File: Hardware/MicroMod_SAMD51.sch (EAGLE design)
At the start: 30 parts, among them J2 MICROMOD-2222, U1 W25QXX6X5, U2 ATSAMD51J20A-A, Y1 32.768kHz

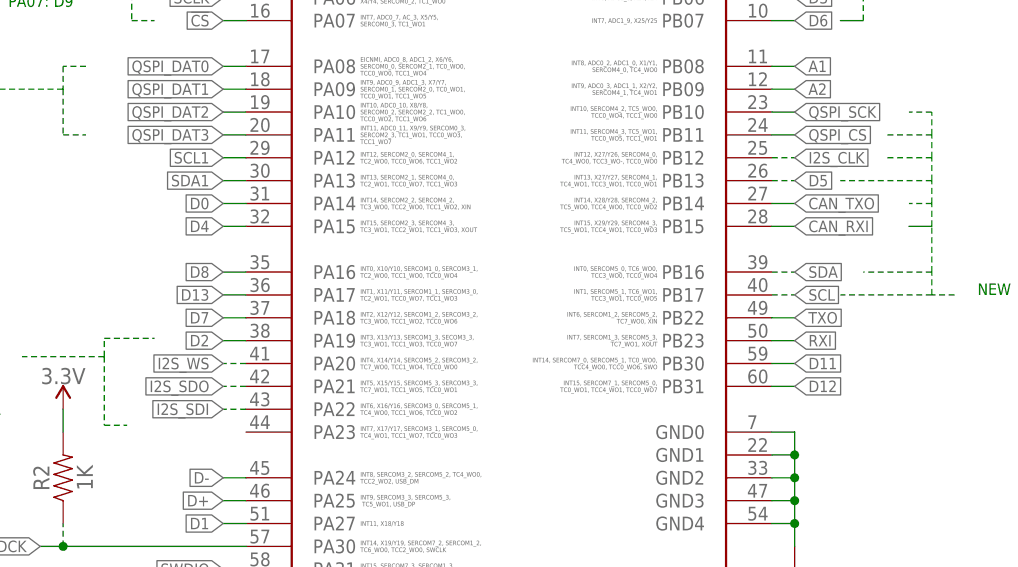
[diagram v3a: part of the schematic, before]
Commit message: Puts i2c on correct pin
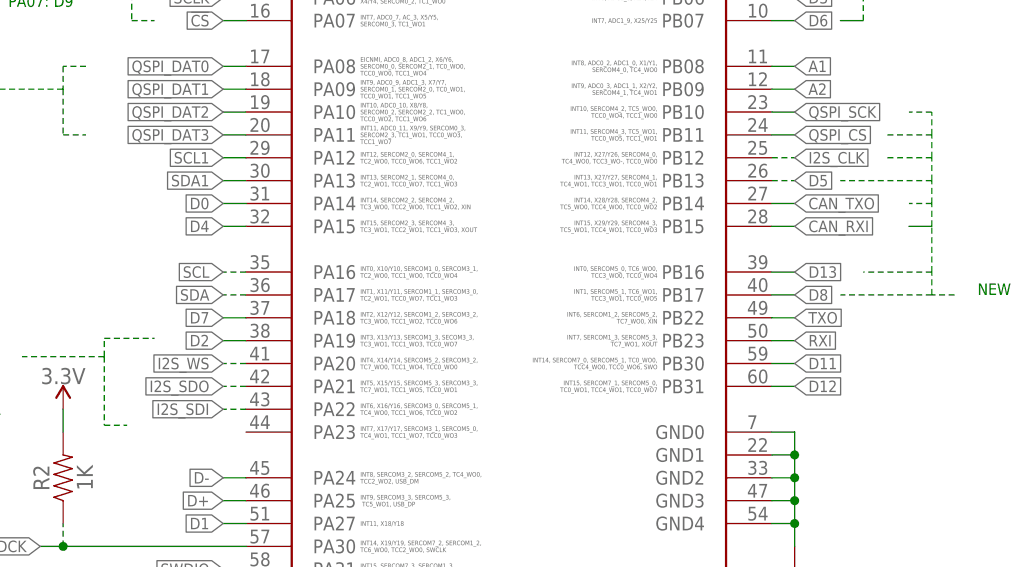
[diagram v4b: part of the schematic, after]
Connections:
- net D13: now also U2.PB16; no longer U2.PA17
- net D8: now also U2.PB17; no longer U2.PA16
- net SCL: now also U2.PA16; no longer U2.PB17
- net SDA: now also U2.PA17; no longer U2.PB16
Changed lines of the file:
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@@
 <net name="D13" class="0">
-<segment>
-<pinref part="U2" gate="G$1" pin="PA17"/>
-<wire x1="93.98" y1="193.04" x2="91.44" y2="193.04" width="0.1524" layer="91"/>
-<label x="91.44" y="193.04" size="1.27" layer="95" font="vector" rot="R180" xref="yes"/>
-</segment>
 <segment>
 <pinref part="R3" gate="G$1" pin="2"/>
@@
 <wire x1="187.96" y1="78.74" x2="185.42" y2="78.74" width="0.1524" layer="91"/>
 <label x="185.42" y="78.74" size="1.27" layer="95" rot="R180" xref="yes"/>
+</segment>
+<segment>
+<wire x1="152.4" y1="195.58" x2="154.94" y2="195.58" width="0.1524" layer="91"/>
+<label x="154.94" y="195.58" size="1.27" layer="95" font="vector" xref="yes"/>
+<pinref part="U2" gate="G$1" pin="PB16"/>
 </segment>
 </net>
@@
 <net name="D8" class="0">
 <segment>
-<pinref part="U2" gate="G$1" pin="PA16"/>
-<wire x1="93.98" y1="195.58" x2="91.44" y2="195.58" width="0.1524" layer="91"/>
-<label x="91.44" y="195.58" size="1.27" layer="95" font="vector" rot="R180" xref="yes"/>
-</segment>
-<segment>
 <wire x1="373.38" y1="165.1" x2="375.92" y2="165.1" width="0.1524" layer="91"/>
 <label x="375.92" y="165.1" size="1.27" layer="95" xref="yes"/>
 <pinref part="J2" gate="J1" pin="G6/BUS6"/>
+</segment>
+<segment>
+<wire x1="152.4" y1="193.04" x2="154.94" y2="193.04" width="0.1524" layer="91"/>
+<label x="154.94" y="193.04" size="1.27" layer="95" font="vector" xref="yes"/>
+<pinref part="U2" gate="G$1" pin="PB17"/>
 </segment>
 </net>
@@
 </segment>
 <segment>
-<pinref part="U2" gate="G$1" pin="PB17"/>
-<wire x1="152.4" y1="193.04" x2="154.94" y2="193.04" width="0.1524" layer="91" style="dashdot"/>
-<label x="154.94" y="193.04" size="1.27" layer="95" xref="yes"/>
+<wire x1="93.98" y1="195.58" x2="91.44" y2="195.58" width="0.1524" layer="91" style="dashdot"/>
+<label x="91.44" y="195.58" size="1.27" layer="95" rot="R180" xref="yes"/>
+<pinref part="U2" gate="G$1" pin="PA16"/>
 </segment>
 </net>
@@
 </segment>
 <segment>
-<pinref part="U2" gate="G$1" pin="PB16"/>
-<wire x1="152.4" y1="195.58" x2="154.94" y2="195.58" width="0.1524" layer="91" style="dashdot"/>
-<label x="154.94" y="195.58" size="1.27" layer="95" xref="yes"/>
+<wire x1="93.98" y1="193.04" x2="91.44" y2="193.04" width="0.1524" layer="91" style="dashdot"/>
+<label x="91.44" y="193.04" size="1.27" layer="95" rot="R180" xref="yes"/>
+<pinref part="U2" gate="G$1" pin="PA17"/>
 </segment>
 </net>

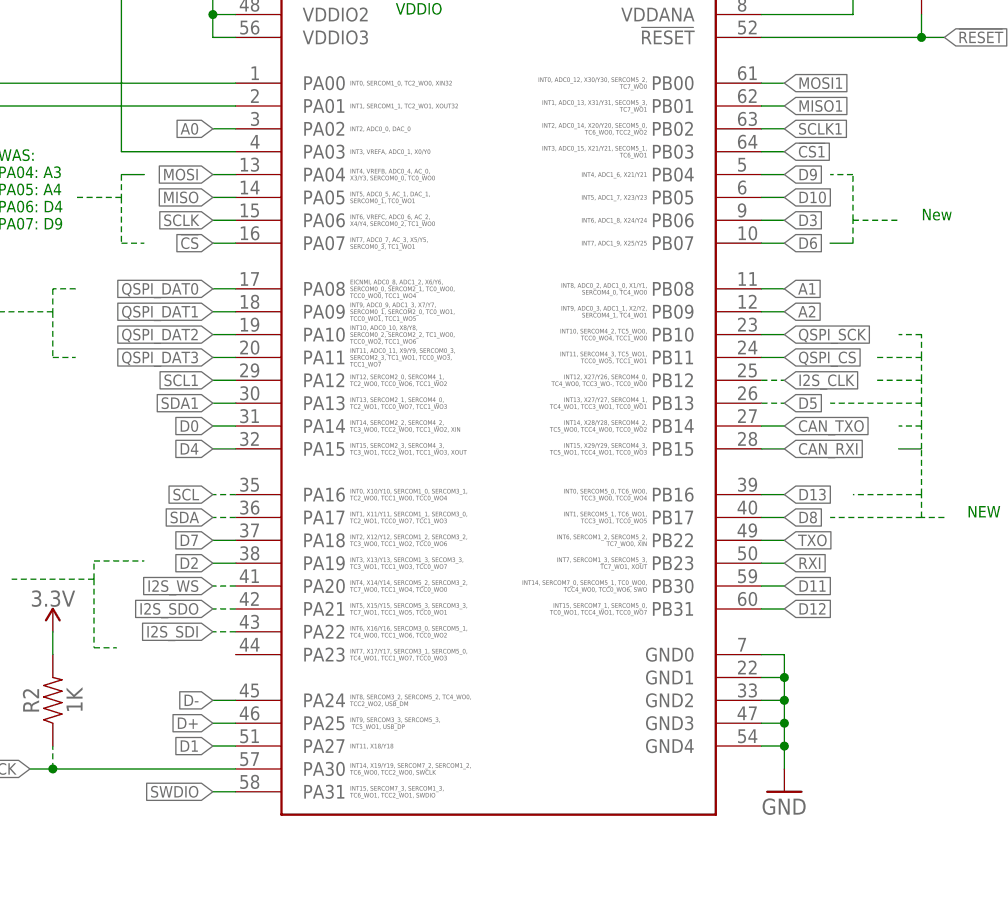
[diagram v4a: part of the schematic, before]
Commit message: Renumbers pins
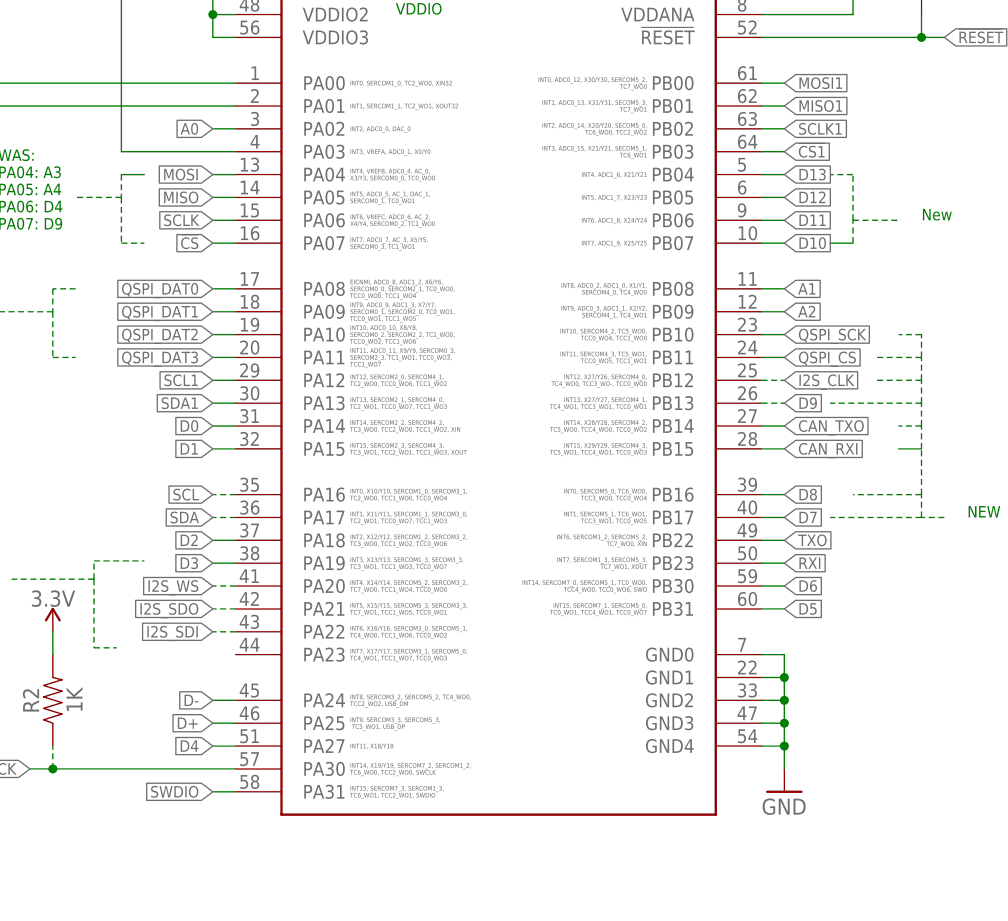
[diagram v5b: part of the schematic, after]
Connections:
- net D1: now also U2.PA15; no longer U2.PA27
- net D10: now also U2.PB07; no longer U2.PB05
- net D11: now also U2.PB06; no longer U2.PB30
- net D12: now also U2.PB05; no longer U2.PB31
- net D13: now also U2.PB04; no longer U2.PB16
- net D2: now also U2.PA18; no longer U2.PA19
- net D3: now also U2.PA19; no longer U2.PB06
- net D4: now also U2.PA27; no longer U2.PA15
- net D5: now also U2.PB31; no longer U2.PB13
- net D6: now also U2.PB30; no longer U2.PB07
- net D7: now also U2.PB17; no longer U2.PA18
- net D8: now also U2.PB16; no longer U2.PB17
- net D9: now also U2.PB13; no longer U2.PB04

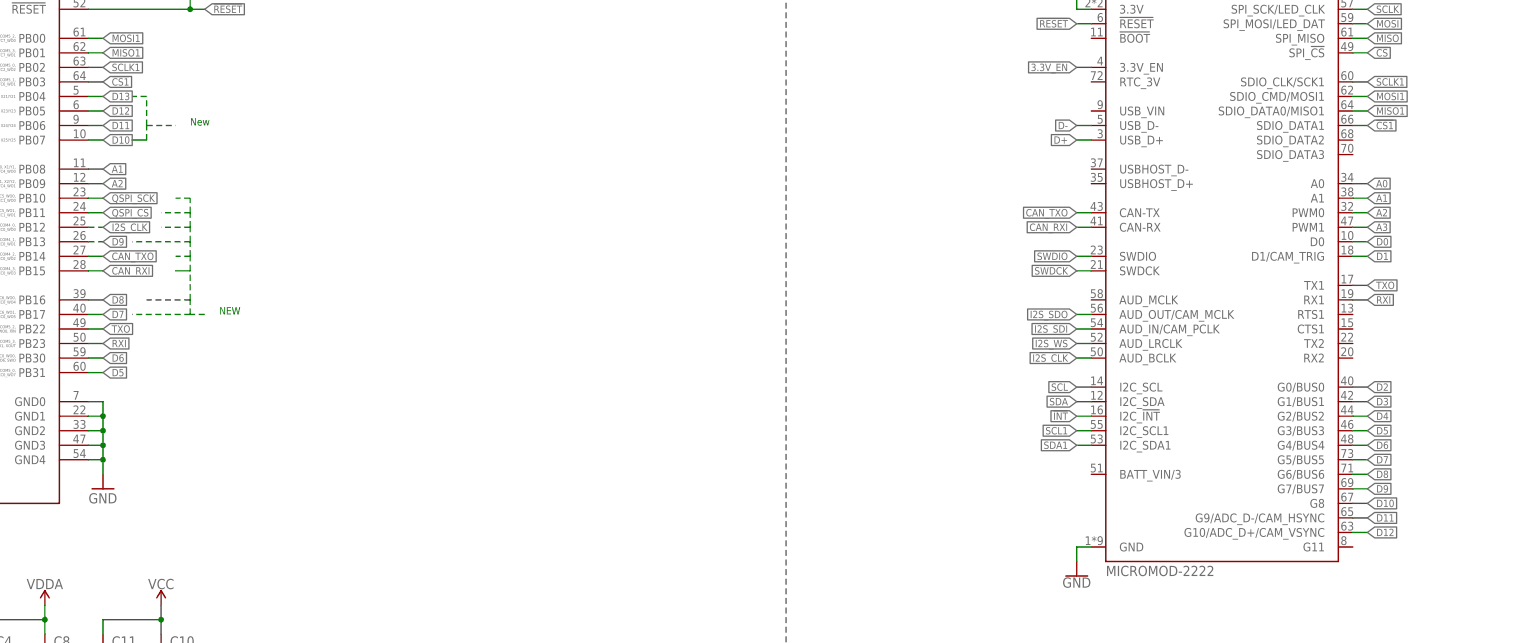
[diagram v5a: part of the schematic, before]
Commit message: Adds A3 to SAMD51, adds PWM to A2 and A3 net names
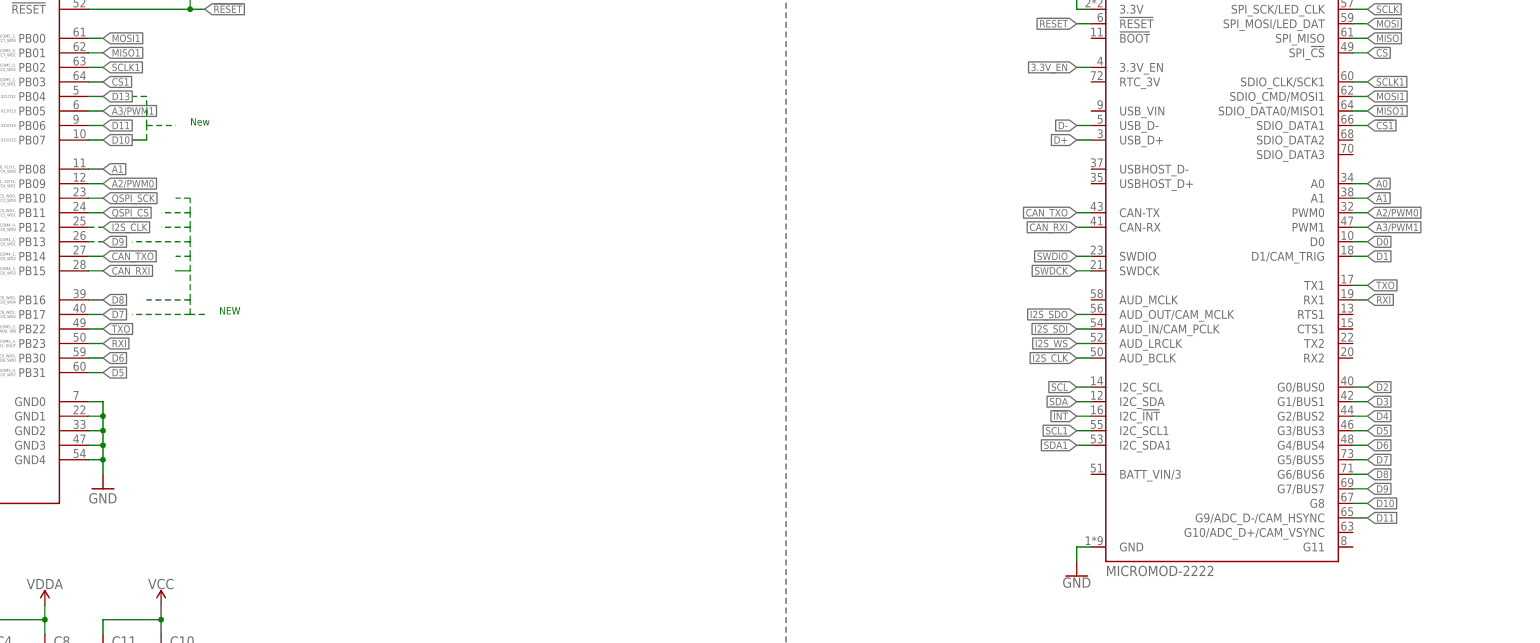
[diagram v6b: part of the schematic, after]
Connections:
- net A2 renamed A2/PWM0
- removed net A3: J2.PWM1
- removed net D12: J2.G10/ADC_D+/CAM_VSYNC, U2.PB05
- new net A3/PWM1: J2.PWM1, U2.PB05
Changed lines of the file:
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@@
-</segment>
-</net>
-<net name="A2" class="0">
-<segment>
-<pinref part="U2" gate="G$1" pin="PB09"/>
-<wire x1="152.4" y1="215.9" x2="154.94" y2="215.9" width="0.1524" layer="91"/>
-<label x="154.94" y="215.9" size="1.27" layer="95" font="vector" xref="yes"/>
-</segment>
-<segment>
-<pinref part="J2" gate="J1" pin="PWM0"/>
-<wire x1="373.38" y1="210.82" x2="375.92" y2="210.82" width="0.1524" layer="91"/>
-<label x="375.92" y="210.82" size="1.27" layer="95" xref="yes"/>
 </segment>
 </net>
@@
 </segment>
 </net>
-<net name="A3" class="0">
+<net name="D11" class="0">
+<segment>
+<pinref part="J2" gate="J1" pin="G9/ADC_D-/CAM_HSYNC"/>
+<wire x1="373.38" y1="157.48" x2="375.92" y2="157.48" width="0.1524" layer="91"/>
+<label x="375.92" y="157.48" size="1.27" layer="95" xref="yes"/>
+</segment>
+<segment>
+<pinref part="U2" gate="G$1" pin="PB06"/>
+<wire x1="152.4" y1="226.06" x2="154.94" y2="226.06" width="0.1524" layer="91"/>
+<label x="154.94" y="226.06" size="1.27" layer="95" xref="yes"/>
+</segment>
+</net>
+<net name="A3/PWM1" class="0">
+<segment>
+<pinref part="U2" gate="G$1" pin="PB05"/>
+<wire x1="152.4" y1="228.6" x2="154.94" y2="228.6" width="0.1524" layer="91"/>
+<label x="154.94" y="228.6" size="1.27" layer="95" xref="yes"/>
+</segment>
 <segment>
 <pinref part="J2" gate="J1" pin="PWM1"/>
@@
 </segment>
 </net>
-<net name="D11" class="0">
-<segment>
-<pinref part="J2" gate="J1" pin="G9/ADC_D-/CAM_HSYNC"/>
-<wire x1="373.38" y1="157.48" x2="375.92" y2="157.48" width="0.1524" layer="91"/>
-<label x="375.92" y="157.48" size="1.27" layer="95" xref="yes"/>
-</segment>
-<segment>
-<pinref part="U2" gate="G$1" pin="PB06"/>
-<wire x1="152.4" y1="226.06" x2="154.94" y2="226.06" width="0.1524" layer="91"/>
-<label x="154.94" y="226.06" size="1.27" layer="95" xref="yes"/>
-</segment>
-</net>
-<net name="D12" class="0">
-<segment>
-<pinref part="J2" gate="J1" pin="G10/ADC_D+/CAM_VSYNC"/>
-<wire x1="373.38" y1="154.94" x2="375.92" y2="154.94" width="0.1524" layer="91"/>
-<label x="375.92" y="154.94" size="1.27" layer="95" xref="yes"/>
-</segment>
-<segment>
-<pinref part="U2" gate="G$1" pin="PB05"/>
-<wire x1="152.4" y1="228.6" x2="154.94" y2="228.6" width="0.1524" layer="91"/>
-<label x="154.94" y="228.6" size="1.27" layer="95" xref="yes"/>
-</segment>
-</net>
 <net name="SCL1" class="0">
 <segment>
@@
 </segment>
 </net>
+<net name="A2/PWM0" class="0">
+<segment>
+<pinref part="J2" gate="J1" pin="PWM0"/>
+<wire x1="373.38" y1="210.82" x2="375.92" y2="210.82" width="0.1524" layer="91"/>
+<label x="375.92" y="210.82" size="1.27" layer="95" xref="yes"/>
+</segment>
+<segment>
+<pinref part="U2" gate="G$1" pin="PB09"/>
+<wire x1="152.4" y1="215.9" x2="154.94" y2="215.9" width="0.1524" layer="91"/>
+<label x="154.94" y="215.9" size="1.27" layer="95" font="vector" xref="yes"/>
+</segment>
+</net>

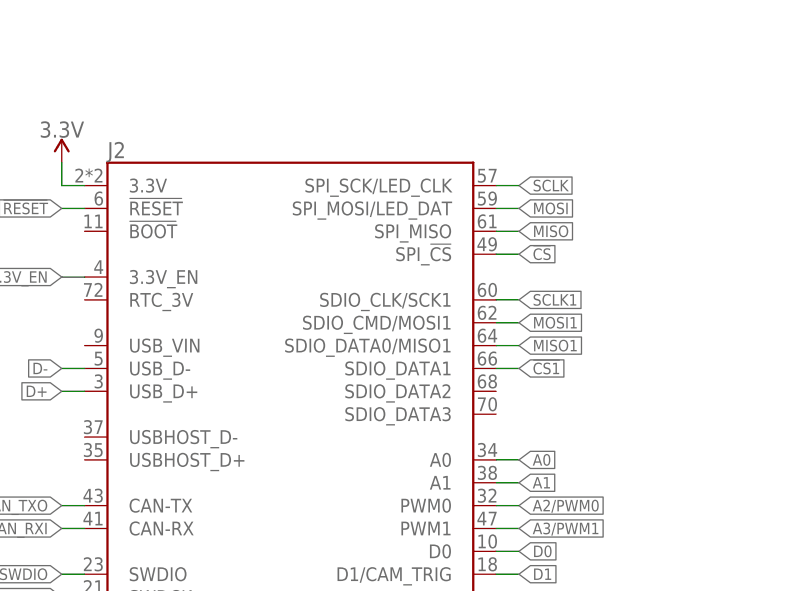
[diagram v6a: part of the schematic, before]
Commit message: Updates Micro mod connector to latest version
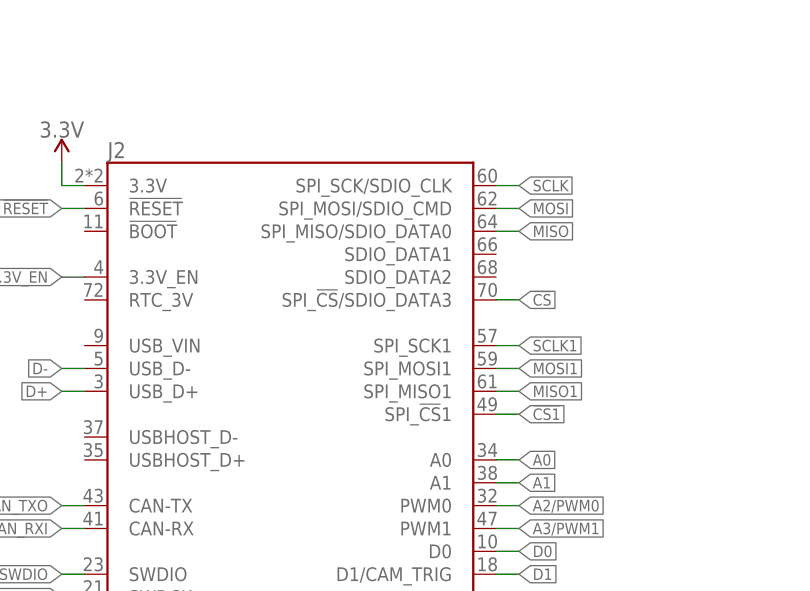
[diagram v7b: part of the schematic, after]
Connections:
- net !CS: now also J2.SPI_!CS!/SDIO_DATA3; no longer J2.SPI_!CS!
- net !CS1: now also J2.SPI_!CS!1; no longer J2.SDIO_DATA1
- net MISO: now also J2.SPI_MISO/SDIO_DATA0; no longer J2.SPI_MISO
- net MISO1: now also J2.SPI_MISO1; no longer J2.SDIO_DATA0/MISO1
- net MOSI: now also J2.SPI_MOSI/SDIO_CMD; no longer J2.SPI_MOSI/LED_DAT
- net MOSI1: now also J2.SPI_MOSI1; no longer J2.SDIO_CMD/MOSI1
- net SCLK: now also J2.SPI_SCK/SDIO_CLK; no longer J2.SPI_SCK/LED_CLK
- net SCLK1: now also J2.SPI_SCK1; no longer J2.SDIO_CLK/SCK1
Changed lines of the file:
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@@
 <net name="MOSI" class="0">
 <segment>
-<pinref part="J2" gate="J1" pin="SPI_MOSI/LED_DAT"/>
+<pinref part="J2" gate="J1" pin="SPI_MOSI/SDIO_CMD"/>
 <wire x1="373.38" y1="243.84" x2="375.92" y2="243.84" width="0.2032" layer="91"/>
 <label x="375.92" y="243.84" size="1.27" layer="95" xref="yes"/>
@@
 <net name="MISO" class="0">
 <segment>
-<pinref part="J2" gate="J1" pin="SPI_MISO"/>
+<pinref part="J2" gate="J1" pin="SPI_MISO/SDIO_DATA0"/>
 <wire x1="373.38" y1="241.3" x2="375.92" y2="241.3" width="0.2032" layer="91"/>
 <label x="375.92" y="241.3" size="1.27" layer="95" xref="yes"/>
@@
 <net name="SCLK" class="0">
 <segment>
-<pinref part="J2" gate="J1" pin="SPI_SCK/LED_CLK"/>
+<pinref part="J2" gate="J1" pin="SPI_SCK/SDIO_CLK"/>
 <wire x1="373.38" y1="246.38" x2="375.92" y2="246.38" width="0.2032" layer="91"/>
 <label x="375.92" y="246.38" size="1.27" layer="95" xref="yes"/>
@@
 <net name="!CS" class="0">
 <segment>
-<pinref part="J2" gate="J1" pin="SPI_!CS!"/>
-<wire x1="373.38" y1="238.76" x2="375.92" y2="238.76" width="0.2032" layer="91"/>
-<label x="375.92" y="238.76" size="1.27" layer="95" xref="yes"/>
-</segment>
-<segment>
 <pinref part="U2" gate="G$1" pin="PA07"/>
 <wire x1="93.98" y1="223.52" x2="91.44" y2="223.52" width="0.1524" layer="91"/>
 <label x="91.44" y="223.52" size="1.27" layer="95" font="vector" rot="R180" xref="yes"/>
+</segment>
+<segment>
+<wire x1="373.38" y1="233.68" x2="375.92" y2="233.68" width="0.2032" layer="91"/>
+<label x="375.92" y="233.68" size="1.27" layer="95" xref="yes"/>
+<pinref part="J2" gate="J1" pin="SPI_!CS!/SDIO_DATA3"/>
 </segment>
 </net>
@@
 </segment>
 <segment>
-<pinref part="J2" gate="J1" pin="SDIO_CMD/MOSI1"/>
-<wire x1="373.38" y1="231.14" x2="375.92" y2="231.14" width="0.1524" layer="91"/>
-<label x="375.92" y="231.14" size="1.27" layer="95" xref="yes"/>
+<wire x1="373.38" y1="226.06" x2="375.92" y2="226.06" width="0.1524" layer="91"/>
+<label x="375.92" y="226.06" size="1.27" layer="95" xref="yes"/>
+<pinref part="J2" gate="J1" pin="SPI_MOSI1"/>
 </segment>
 </net>
@@
 </segment>
 <segment>
-<pinref part="J2" gate="J1" pin="SDIO_DATA0/MISO1"/>
-<wire x1="373.38" y1="228.6" x2="375.92" y2="228.6" width="0.1524" layer="91"/>
-<label x="375.92" y="228.6" size="1.27" layer="95" xref="yes"/>
+<wire x1="373.38" y1="223.52" x2="375.92" y2="223.52" width="0.1524" layer="91"/>
+<label x="375.92" y="223.52" size="1.27" layer="95" xref="yes"/>
+<pinref part="J2" gate="J1" pin="SPI_MISO1"/>
 </segment>
 </net>
@@
 </segment>
 <segment>
-<pinref part="J2" gate="J1" pin="SDIO_CLK/SCK1"/>
-<wire x1="373.38" y1="233.68" x2="375.92" y2="233.68" width="0.1524" layer="91"/>
-<label x="375.92" y="233.68" size="1.27" layer="95" xref="yes"/>
+<wire x1="373.38" y1="228.6" x2="375.92" y2="228.6" width="0.1524" layer="91"/>
+<label x="375.92" y="228.6" size="1.27" layer="95" xref="yes"/>
+<pinref part="J2" gate="J1" pin="SPI_SCK1"/>
 </segment>
 </net>
@@
 </segment>
 <segment>
-<pinref part="J2" gate="J1" pin="SDIO_DATA1"/>
-<wire x1="373.38" y1="226.06" x2="375.92" y2="226.06" width="0.1524" layer="91"/>
-<label x="375.92" y="226.06" size="1.27" layer="95" xref="yes"/>
-</segment>
-</net>
+<wire x1="373.38" y1="220.98" x2="375.92" y2="220.98" width="0.1524" layer="91"/>
+<label x="375.92" y="220.98" size="1.27" layer="95" xref="yes"/>
+<pinref part="J2" gate="J1" pin="SPI_!CS!1"/>
+</segment>
+</net>
